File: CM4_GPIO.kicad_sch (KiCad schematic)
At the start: 27 parts, among them IC5 74LVC1G07QSE-7, J3 2222, SW1 SW_Push, SW2 SW_Push, SW3 SW_Push

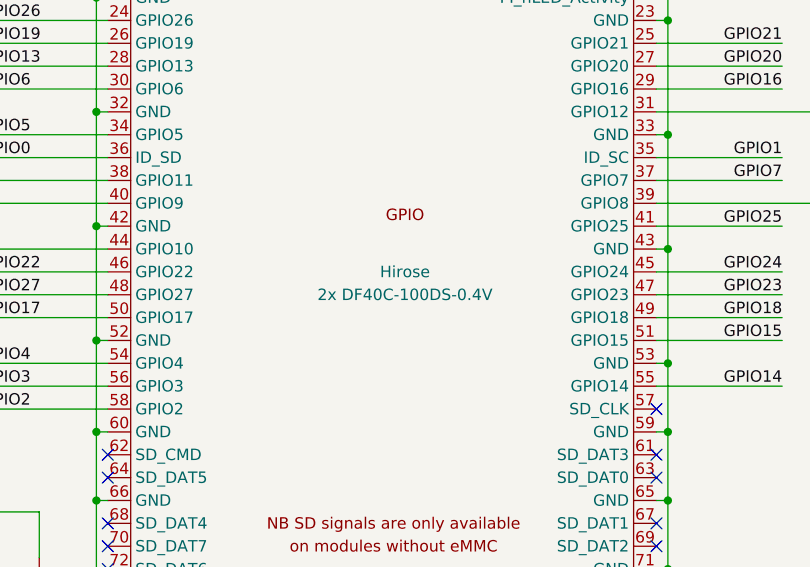
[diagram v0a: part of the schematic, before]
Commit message: changed usb to be simpler (no inbuilt hub)
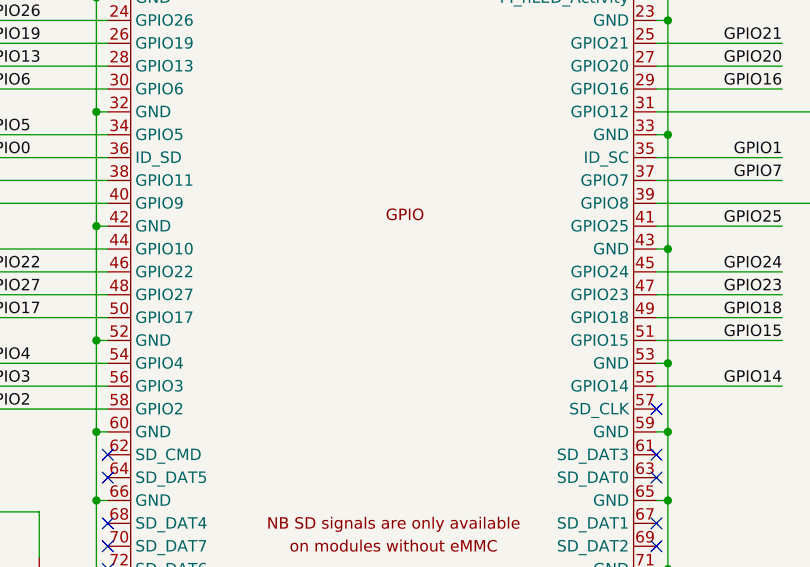
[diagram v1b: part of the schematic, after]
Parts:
- IC5: Arrow Part Number 74LVC1G07QSE-7 -> (none); Arrow Price/Stock https://www.arrow.com/en/products/74lvc1g07qse-7/diodes-inc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 -> (none); Height 1.1 -> (none); Manufacturer_Name Diodes Incorporated -> (none); Manufacturer_Part_Number 74LVC1G07QSE-7 -> (none); Mouser Part Number 621-74LVC1G07QSE-7 -> (none); Mouser Price/Stock https://www.mouser.co.uk/ProductDetail/Diodes-Incorporated/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 -> (none)
- Module1: Field4 Hirose -> (none); Field5 2x DF40C-100DS-0.4V -> (none)
- S1, S2: Height 3.5 -> (none)
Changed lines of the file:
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@@
-			)
-		)
-		(property "Height" "1.1"
-			(at 196.85 444.45 0)
-			(effects
-				(font
-					(size 1.27 1.27)
-				)
-				(justify left top)
-				(hide yes)
-			)
-		)
-		(property "Manufacturer_Name" "Diodes Incorporated"
-			(at 196.85 544.45 0)
-			(effects
-				(font
-					(size 1.27 1.27)
-				)
-				(justify left top)
-				(hide yes)
-			)
-		)
-		(property "Manufacturer_Part_Number" "74LVC1G07QSE-7"
-			(at 196.85 644.45 0)
-			(effects
-				(font
-					(size 1.27 1.27)
-				)
-				(justify left top)
-				(hide yes)
-			)
-		)
-		(property "Mouser Part Number" "621-74LVC1G07QSE-7"
-			(at 196.85 744.45 0)
-			(effects
-				(font
-					(size 1.27 1.27)
-				)
-				(justify left top)
-				(hide yes)
-			)
-		)
-		(property "Mouser Price/Stock" "https://www.mouser.co.uk/ProductDetail/Diodes-Incorporated/74LVC1G07QSE-7?qs=P1JMDcb91o6kX7wpGC%252Bbgg%3D%3D"
-			(at 196.85 844.45 0)
-			(effects
-				(font
-					(size 1.27 1.27)
-				)
-				(justify left top)
-				(hide yes)
-			)
-		)
-		(property "Arrow Part Number" "74LVC1G07QSE-7"
-			(at 196.85 944.45 0)
-			(effects
-				(font
-					(size 1.27 1.27)
-				)
-				(justify left top)
-				(hide yes)
-			)
-		)
-		(property "Arrow Price/Stock" "https://www.arrow.com/en/products/74lvc1g07qse-7/diodes-incorporated?region=nac"
-			(at 196.85 1044.45 0)
-			(effects
-				(font
-					(size 1.27 1.27)
-				)
-				(justify left top)
-				(hide yes)
 			)
 		)
@@
 			)
 		)
-		(property "Height" "3.5"
-			(at 139.7 575.26 0)
-			(effects
-				(font
-					(size 1.27 1.27)
-				)
-				(justify left top)
-				(hide yes)
-			)
-		)
 		(pin "3"
 		)
@@
 		(property "P/N" "DF40C-100DS-0.4V"
 			(at 83.82 20.32 0)
-			(effects
-				(font
-					(size 1.27 1.27)
-				)
-			)
-		)
-		(property "Field4" "Hirose"
-			(at 86.36 83.82 0)
-			(effects
-				(font
-					(size 1.27 1.27)
-				)
-			)
-		)
-		(property "Field5" "2x DF40C-100DS-0.4V"
-			(at 86.36 86.36 0)
 			(effects
 				(font
@@
 			(effects
 				(font
-					(size 1.27 1.27)
-				)
-				(justify left top)
-				(hide yes)
-			)
-		)
-		(property "Height" "3.5"
-			(at 57.15 576.53 0)
-			(effects
-				(font

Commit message: moved everything to front & 0603'd stuff
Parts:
- C22, C23, C51: footprint Capacitor_SMD:C_0805_2012Metric -> Capacitor_SMD:C_0603_1608Metric
- D1, D2, D5: footprint LED_SMD:LED_0805_2012Metric -> LED_SMD:LED_0603_1608Metric
- R1, R17, R18, R19, R21, R22, R23, R25, R26, R29, R4: footprint Resistor_SMD:R_0805_2012Metric -> Resistor_SMD:R_0603_1608Metric
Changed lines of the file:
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@@
 			)
 		)
-		(property "Footprint" "Resistor_SMD:R_0805_2012Metric"
+		(property "Footprint" "Resistor_SMD:R_0603_1608Metric"
 			(at 178.562 83.82 90)
 			(effects
@@
 			)
 		)
-		(property "Footprint" "Resistor_SMD:R_0805_2012Metric"
+		(property "Footprint" "Resistor_SMD:R_0603_1608Metric"
 			(at 171.45 91.948 90)
 			(effects
@@
 			)
 		)
-		(property "Footprint" "Resistor_SMD:R_0805_2012Metric"
+		(property "Footprint" "Resistor_SMD:R_0603_1608Metric"
 			(at 224.79 118.618 90)
 			(effects
@@
 			)
 		)
-		(property "Footprint" "Resistor_SMD:R_0805_2012Metric"
+		(property "Footprint" "Resistor_SMD:R_0603_1608Metric"
 			(at 263.652 118.11 90)
 			(effects
@@
 			)
 		)
-		(property "Footprint" "Resistor_SMD:R_0805_2012Metric"
+		(property "Footprint" "Resistor_SMD:R_0603_1608Metric"
 			(at 179.832 129.54 90)
 			(effects
@@
 			)
 		)
-		(property "Footprint" "Capacitor_SMD:C_0805_2012Metric"
+		(property "Footprint" "Capacitor_SMD:C_0603_1608Metric"
 			(at 182.5752 143.51 0)
 			(effects
@@
 			)
 		)
-		(property "Footprint" "Resistor_SMD:R_0805_2012Metric"
+		(property "Footprint" "Resistor_SMD:R_0603_1608Metric"
 			(at 193.802 43.18 90)
 			(effects
@@
 			)
 		)
-		(property "Footprint" "LED_SMD:LED_0805_2012Metric"
+		(property "Footprint" "LED_SMD:LED_0603_1608Metric"
 			(at 195.58 26.67 0)
 			(effects
@@
 			)
 		)
-		(property "Footprint" "Resistor_SMD:R_0805_2012Metric"
+		(property "Footprint" "Resistor_SMD:R_0603_1608Metric"
 			(at 126.492 48.26 90)
 			(effects
@@
 			)
 		)
-		(property "Footprint" "LED_SMD:LED_0805_2012Metric"
+		(property "Footprint" "LED_SMD:LED_0603_1608Metric"
 			(at 265.43 127 0)
 			(effects
@@
 			)
 		)
-		(property "Footprint" "Resistor_SMD:R_0805_2012Metric"
+		(property "Footprint" "Resistor_SMD:R_0603_1608Metric"
 			(at 36.322 119.38 90)
 			(effects
@@
 			)
 		)
-		(property "Footprint" "Resistor_SMD:R_0805_2012Metric"
+		(property "Footprint" "Resistor_SMD:R_0603_1608Metric"
 			(at 231.902 110.49 90)
 			(effects
@@
 			)
 		)
-		(property "Footprint" "Resistor_SMD:R_0805_2012Metric"
+		(property "Footprint" "Resistor_SMD:R_0603_1608Metric"
 			(at 43.942 119.38 90)
 			(effects
@@
 			)
 		)
-		(property "Footprint" "Capacitor_SMD:C_0805_2012Metric"
+		(property "Footprint" "Capacitor_SMD:C_0603_1608Metric"
 			(at 234.6452 124.46 0)
 			(effects
@@
 			)
 		)
-		(property "Footprint" "LED_SMD:LED_0805_2012Metric"
+		(property "Footprint" "LED_SMD:LED_0603_1608Metric"
 			(at 128.27 36.83 0)
 			(effects
@@
 			)
 		)
-		(property "Footprint" "Capacitor_SMD:C_0805_2012Metric"
+		(property "Footprint" "Capacitor_SMD:C_0603_1608Metric"
 			(at 181.3052 97.79 0)
 			(effects
@@
 			)
 		)
-		(property "Footprint" "Resistor_SMD:R_0805_2012Metric"
+		(property "Footprint" "Resistor_SMD:R_0603_1608Metric"
 			(at 172.72 137.668 90)
 			(effects

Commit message: changed a bunch of stuff, still have work
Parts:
- added TP4: TestPoint, TestPoint:TestPoint_Pad_2.0x2.0mm, symbol Connector:TestPoint
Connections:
- net +1.8V: now reaches Module1.88 (+1.8v_(Output))
- net +1.8V: now also Module1.90 (+1.8v_(Output)), TP4.1
- no-connect marks 35 -> 33
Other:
- note added: ""GPIO load should be kept below 50mA""
- note added: "More LEDS"
- note added: "fwd cur: ~2ma fwd volt: ~2V R: ~650-700"
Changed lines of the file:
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@@
 		)
 	)
+	(text "More LEDS"
+		(exclude_from_sim no)
+		(at 133.096 119.634 0)
+		(effects
+			(font
+				(size 2 2)
+			)
+		)
+	)
+	(text "fwd cur: ~2ma\nfwd volt: ~2V\nR: ~650-700"
+		(exclude_from_sim no)
+		(at 275.59 111.506 0)
+		(effects
+			(font
+				(size 1.27 1.27)
+			)
+		)
+	)
 	(text "Hard Reset Button"
 		(exclude_from_sim no)
@@
 		)
 	)
+	(text "\"GPIO load should be kept\nbelow 50mA\""
+		(exclude_from_sim no)
+		(at 35.306 20.828 0)
+		(effects
+			(font
+				(size 2 2)
+			)
+		)
+	)
 	(junction
 		(at 115.57 35.56)
@@
 	)
 	(junction
+		(at 53.34 137.16)
+		(diameter 0)
+		(color 0 0 0 0)
+	)
+	(junction
 		(at 45.72 129.54)
 		(diameter 0)
@@
 	)
 	(no_connect
-		(at 53.34 139.7)
-	)
-	(no_connect
 		(at 53.34 111.76)
 	)
@@
 	)
 	(no_connect
-		(at 53.34 137.16)
-	)
-	(no_connect
 		(at 114.3 99.06)
 	)
@@
 	(wire
 		(pts
+			(xy 53.34 137.16) (xy 53.34 139.7)
+		)
+		(stroke
+			(width 0)
+			(type default)
+		)
+	)
+	(wire
+		(pts
 			(xy 115.57 116.84) (xy 115.57 156.21)
 		)
@@
 	(wire
 		(pts
+			(xy 48.26 137.16) (xy 53.34 137.16)
+		)
+		(stroke
+			(width 0)
+			(type default)
+		)
+	)
+	(wire
+		(pts
 			(xy 52.07 149.86) (xy 52.07 157.48)
 		)
@@
 	)
 	(symbol
+		(lib_id "power:+3.3V")
+		(at 48.26 137.16 90)
+		(unit 1)
+		(exclude_from_sim no)
+		(in_bom yes)
+		(on_board yes)
+		(dnp no)
+		(property "Reference" "#PWR05"
+			(at 52.07 137.16 0)
+			(effects
+				(font
+					(size 1.27 1.27)
+				)
+				(hide yes)
+			)
+		)
+		(property "Value" "+1.8V"
+			(at 44.45 137.414 0)
+			(effects
+				(font
+					(size 1.27 1.27)
+				)
+			)
+		)
+		(property "Footprint" ""
+			(at 48.26 137.16 0)
+			(effects
+				(font
+					(size 1.27 1.27)
+				)
+				(hide yes)
+			)
+		)
+		(property "Datasheet" ""
+			(at 48.26 137.16 0)
+			(effects
+				(font
+					(size 1.27 1.27)
+				)
+				(hide yes)
+			)
+		)
+		(property "Description" "Power symbol creates a global label with name \"+3.3V\""
+			(at 48.26 137.16 0)
+			(effects
+				(font
+					(size 1.27 1.27)
+				)
+				(hide yes)
+			)
+		)
+		(pin "1"
+		)
+		(instances
+			(project ""
+				(path "/e4d65698-b8ec-4bf6-9f2b-a5010377155a/353ee88d-a044-4c9d-80a8-948975426026"
+					(reference "#PWR05")
+					(unit 1)
+				)
+			)
+		)
+	)
+	(symbol
 		(lib_id "Device:R")
 		(at 180.34 83.82 0)
@@
 	)
 	(symbol
+		(lib_id "power:+3.3V")
+		(at 204.47 156.21 0)
+		(unit 1)
+		(exclude_from_sim no)
+		(in_bom yes)
+		(on_board yes)
+		(dnp no)
+		(property "Reference" "#PWR018"
+			(at 204.47 160.02 0)
+			(effects
+				(font
+					(size 1.27 1.27)
+				)
+				(hide yes)
+			)
+		)
+		(property "Value" "+1.8V"
+			(at 204.216 152.4 0)
+			(effects
+				(font
+					(size 1.27 1.27)
+				)
+			)
+		)
+		(property "Footprint" ""
+			(at 204.47 156.21 0)
+			(effects
+				(font
+					(size 1.27 1.27)
+				)
+				(hide yes)
+			)
+		)
+		(property "Datasheet" ""
+			(at 204.47 156.21 0)
+			(effects
+				(font
+					(size 1.27 1.27)
+				)
+				(hide yes)
+			)
+		)
+		(property "Description" "Power symbol creates a global label with name \"+3.3V\""
+			(at 204.47 156.21 0)
+			(effects
+				(font
+					(size 1.27 1.27)
+				)
+				(hide yes)
+			)
+		)
+		(pin "1"
+		)
+		(instances
+			(project "PiBoard"
+				(path "/e4d65698-b8ec-4bf6-9f2b-a5010377155a/353ee88d-a044-4c9d-80a8-948975426026"
+					(reference "#PWR018")
+					(unit 1)
+				)
+			)
+		)
+	)
+	(symbol
 		(lib_id "Device:R")
 		(at 233.68 110.49 0)
@@
 					(unit 1)
 				)
+			)
+		)
+	)
+	(symbol
+		(lib_id "Connector:TestPoint")
+		(at 204.47 156.21 180)
+		(unit 1)
+		(exclude_from_sim no)
+		(in_bom yes)
+		(on_board yes)
+		(dnp no)
+		(property "Reference" "TP4"
+			(at 201.803 158.5722 90)
+			(effects
+				(font
+					(size 1.27 1.27)
+				)
+				(justify left)
+			)
+		)
+		(property "Value" "TestPoint"
+			(at 206.883 153.4922 90)
+			(effects
+				(font
+					(size 1.27 1.27)
+				)
+				(justify left)
+			)
+		)
+		(property "Footprint" "TestPoint:TestPoint_Pad_2.0x2.0mm"
+			(at 199.39 156.21 0)
+			(effects
+				(font
+					(size 1.27 1.27)
+				)
+				(hide yes)
+			)
+		)
+		(property "Datasheet" "~"
+			(at 199.39 156.21 0)
+			(effects
+				(font
+					(size 1.27 1.27)
+				)
+				(hide yes)
+			)
+		)
+		(property "Description" "test point"
+			(at 204.47 156.21 0)
+			(effects
+				(font
+					(size 1.27 1.27)
+				)
+				(hide yes)
+			)
+		)
+		(pin "1"
+		)
+		(instances
+			(project "PiBoard"
+				(path "/e4d65698-b8ec-4bf6-9f2b-a5010377155a/353ee88d-a044-4c9d-80a8-948975426026"
+					(reference "TP4")
+					(unit 1)
+				)

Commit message: poop
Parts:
- added D13: HBT, LED_SMD:LED_0603_1608Metric, symbol Device:LED
- added D14: FAULT, LED_SMD:LED_0603_1608Metric, symbol Device:LED
- added D16: STUFF, LED_SMD:LED_0603_1608Metric, symbol Device:LED
- added R15, R20, R33: 700, Resistor_SMD:R_0603_1608Metric, symbol Device:R
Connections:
- net +3.3V_PWR: now also D13.2 (A), D14.2 (A), D16.2 (A)
- net GPIO13: now also R20.2
- net GPIO19: now also R15.2
- net GPIO26: now also R33.2
- new net: D14.1 (K), R20.1
- new net: D16.1 (K), R33.1
- new net: D13.1 (K), R15.1
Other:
- note added: "Ok to be neg-log? If no, may need fets? or we ok with load"

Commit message: my life is horrible
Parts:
- removed C51: 100n, Capacitor_SMD:C_0603_1608Metric, symbol Device:C
- removed IC5: 74LVC1G07QSE-7, Controls_Pi:SOT65P210X110-5N, symbol 74LVC1G07QSE-7:74LVC1G07QSE-7
- removed Module1: ComputeModule4-CM4, CM4IO:Raspberry-Pi-4-Compute-Module, symbol CM4IO:ComputeModule4-CM4
- removed R18, R21, R23, R26, R29: 10k, Resistor_SMD:R_0603_1608Metric, symbol Device:R
- removed R22: 1k, Resistor_SMD:R_0603_1608Metric, symbol Device:R
- removed SW3: SW_Push, Button_Switch_SMD:SW_SPST_B3SL-1002P, symbol Switch:SW_Push
- removed TP1, TP2: TestPoint, TestPoint:TestPoint_Pad_2.0x2.0mm, symbol Connector:TestPoint
- added BT2: Battery_Cell, symbol Device:Battery_Cell
- added J11: RTC Battery Port, Controls_Pi:CONN02_530470210_MOL, symbol 530470210:530470210
- added J12: RTC Battery Conn, Controls_Pi:CONN02_530470210_MOL, symbol 530470210:530470210
- added J14: 4x nano-fit, Connector_JST:JST_SH_BM04B-SRSS-TB_1x04-1MP_P1.00mm_Vertical, symbol Connector_Generic:Conn_01x04
- added Module2: ComputeModule5-CM5, CM5IO:Raspberry-Pi-5-Compute-Module, symbol CM5IO:ComputeModule5-CM5
- added R42: 1k, Resistor_SMD:R_0603_1608Metric, symbol Device:R
- D1: value Activity LED -> Activity
- D2: value PI PWR LED -> PI PWR
- D5: value 3.3V PWR LED -> 3.3V PWR
- R17, R19: value 1k -> 10k
- R4: value 1k -> 10K 1%; Field4 (none) -> Farnell; Field6 (none) -> MCR01MZPF1002; Field7 (none) -> Rohm; P/N CRCW08051K00FKEAC -> (none); Part Description (none) -> Resistor 10K M1005 1% 63mW
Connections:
- net +1.8V: now also Module2.88 (+1.8v_(Output)), Module2.90 (+1.8v_(Output))
- net BT_Disable: now also Module2.91 (BT_nDisable)
- net CAN_INTR: now also Module2.31 (GPIO12)
- net CAN_SPI_CLK: now also Module2.38 (GPIO11)
- net CAN_SPI_CS: now also Module2.39 (GPIO8)
- net CAN_SPI_MISO: now also Module2.40 (GPIO9)
- net CAN_SPI_MOSI: now also Module2.44 (GPIO10)
- net EEPROM_nWP: now also Module2.20 (EEPROM_nWP)
- net GLOBAL_EN: now also Module2.99 (PMIC_ENABLE)
- net GND: now also R25.2, J11.2 (BLK), J14.3 (Pin_3), Module2.1 (GND), Module2.13 (GND), Module2.14 (GND), Module2.2 (GND), Module2.22 (GND), Module2.23 (GND), Module2.32 (GND), Module2.33 (GND), Module2.42 (GND), Module2.43 (GND), Module2.52 (GND), Module2.53 (GND), Module2.59 (GND), Module2.60 (GND), Module2.65 (GND), Module2.66 (GND), Module2.7 (GND), Module2.71 (GND), Module2.74 (GND), Module2.8 (GND), Module2.98 (GND); no longer D5.1 (K)
- net GPIO0: now also Module2.36 (ID_SD)
- net GPIO1: now also Module2.35 (ID_SC)
- net GPIO13: now also Module2.28 (GPIO13)
- net GPIO14: now also Module2.55 (GPIO14)
- net GPIO15: now also Module2.51 (GPIO15)
- net GPIO16: now also Module2.29 (GPIO16)
- net GPIO17: now also Module2.50 (GPIO17)
- net GPIO18: now also Module2.49 (GPIO18)
- net GPIO19: now also Module2.26 (GPIO19)
- net GPIO2: now also Module2.58 (GPIO2)
- net GPIO20: now also Module2.27 (GPIO20)
- net GPIO21: now also Module2.25 (GPIO21)
- net GPIO22: now also Module2.46 (GPIO22)
- net GPIO23: now also Module2.47 (GPIO23)
- net GPIO24: now also Module2.45 (GPIO24)
- net GPIO25: now also Module2.41 (GPIO25)
- net GPIO26: now also Module2.24 (GPIO26)
- net GPIO27: now also Module2.48 (GPIO27)
- net GPIO3: now also Module2.56 (GPIO3)
- net GPIO4: now also Module2.54 (GPIO4)
- net GPIO5: now also Module2.34 (GPIO5)
- net GPIO6: now also Module2.30 (GPIO6)
- net GPIO7: now also Module2.37 (GPIO7)
- net WiFi_Disable: now also Module2.89 (WiFi_nDisable)
- net nPWR_LED: now also Module2.95 (LED_nPWR), R42.2
- net nRPIBOOT: now also Module2.93 (nRPIBOOT)
- net +3.3V: now reaches D5.2 (A)
- net +3.3V: now also D1.2 (A), D13.2 (A), D14.2 (A), D16.2 (A), D2.2 (A), J3.1 (Pin_1), J3.17 (Pin_17), R4.2, Module2.78 (GPIO_VREF(1.8v/3.3v_Input)), Module2.84 (+3.3v_(Output)), Module2.86 (+3.3v_(Output)); no longer R25.2
- net at D2.1 (K): now also R42.1; no longer R4.1
- net LED_nACT: now reaches R1.2
- net LED_nACT: now also Module2.21 (LED_nACT)
- removed net +3.3V_PWR: D1.2 (A), D13.2 (A), D14.2 (A), D16.2 (A), D2.2 (A), J3.1 (Pin_1), J3.17 (Pin_17), R25.1
- net +5V_PWR renamed +5V
- net +5V: now also Module2.77 (+5v_(Input)), Module2.79 (+5v_(Input)), Module2.81 (+5v_(Input)), Module2.83 (+5v_(Input)), Module2.85 (+5v_(Input)), Module2.87 (+5v_(Input))
- net RUN_PG renamed PWR_BUTT
- net PWR_BUTT: now also Module2.92 (PWR_BUT)
- new net: D5.1 (K), R25.1
- new net +24V: J14.1 (Pin_1)
- new net BLK: BT2.2 (-), J12.2 (BLK)
- new net CC1: Module2.94 (CC1)
- new net CC2: Module2.96 (CC2)
- new net FAN_PWM: J14.2 (Pin_2), Module2.19 (FAN_PWM), R4.1
- new net FAN_TACHO: J14.4 (Pin_4), Module2.16 (FAN_TACHO)
- new net RED: BT2.1 (+), J12.1 (RED)
- new net RTC_Batt: J11.1 (RED), Module2.76 (VBAT)
- no-connect marks 33 -> 31
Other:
- note added: "40-pin GPIO Header"
- note added: "BUTTS & SW"
- note added: "Battery is enclosed in a non-SMD holder to mitigate vibration concerns. This is technically an off-board section that has the 2032 coin cell, the battery holder, and the molex connector (male)."
- note added: "CM5 GPIO CONN"
- note added: "Double check this for sanity"
- note added: "FAN connector"
- note added: "For USB PD"
- note added: "Global En"
- note added: "Hard Reset"
- note added: "LEDS"
- note added: "Power Button"
- note added: "Press once for it to wake, sleep, or soft shutdown. Press and hold for hard shutdown."
- note added: "R2 : Pullup added for Fans that don't have a strong internal pullup"
- note added: "RTC BATT"
- note removed: ""GPIO load should be kept below 50mA""
- note removed: "40Way GPIO Header"
- note removed: "Full Reset Button"
- note removed: "Hard Reset Button"
- note removed: "I2C Pullups"
- note removed: "More LEDS"
- note removed: "Ok to be neg-log? If no, may need fets? or we ok with load"
- note removed: "Power LED must be buffered"
- note removed: "Press for >1 ms and then release to reset only the CM4 and any components connected to it (3.3V components). For CM5, this is the shutdown button; press once for it to wake, sleep, or soft shutdown. Press and hold for hard shutdown."
- note removed: "Press for >1 ms and then release to send a shutdown signal and safely shutdown."
- note removed: "Soft Reset Button"
- moved on the sheet: C22, C23, D13, D14, D16, D5, J3, R15, R17, R19, R20, R25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
